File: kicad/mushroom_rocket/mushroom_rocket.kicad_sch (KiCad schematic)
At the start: 6 parts, among them SW1 SW_DIP_x01

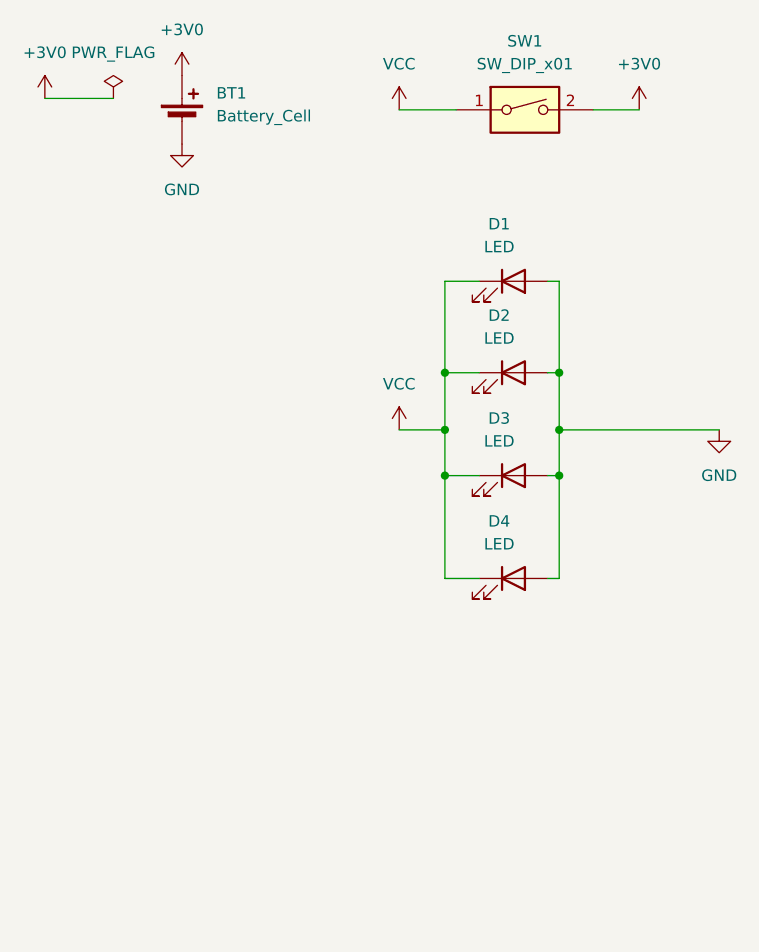
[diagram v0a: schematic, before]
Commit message: added a random pad into the footprint
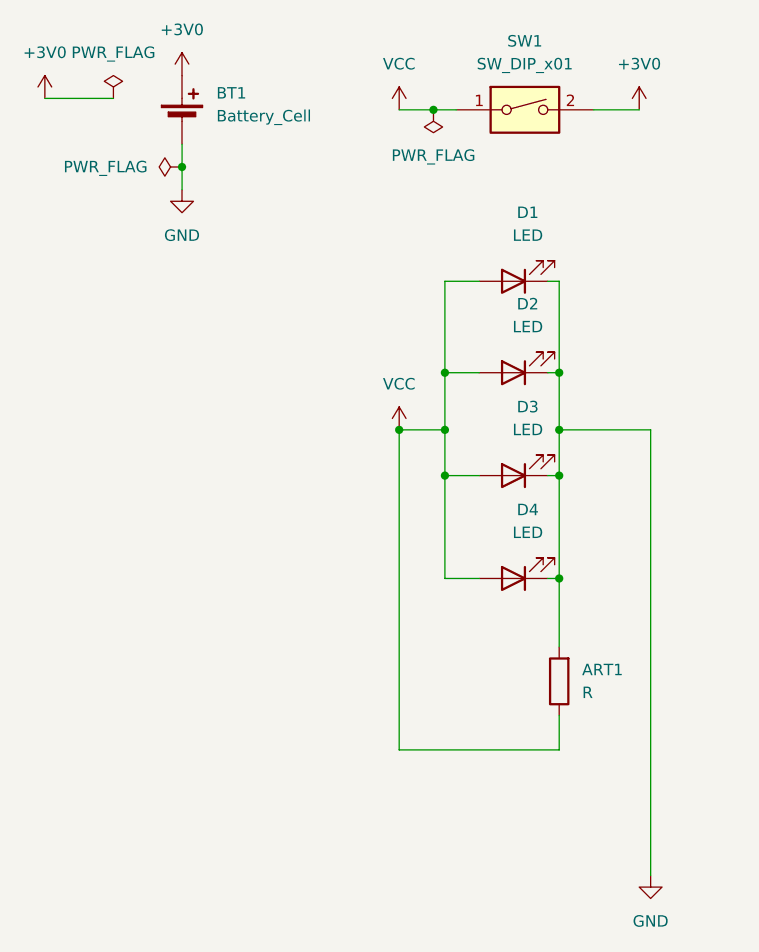
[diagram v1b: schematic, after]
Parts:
- added ART1: R, Mushroom:Footprint_Mushroom_v0.6, symbol Device:R
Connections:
- net GND: now also D1.1 (K), D2.1 (K), D3.1 (K), D4.1 (K), ART1.2; no longer D1.2 (A), D2.2 (A), D3.2 (A), D4.2 (A)
- net VCC: now also D1.2 (A), D2.2 (A), D3.2 (A), D4.2 (A), ART1.1; no longer D1.1 (K), D2.1 (K), D3.1 (K), D4.1 (K)
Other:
- moved on the sheet: D1, D2, D3, D4
